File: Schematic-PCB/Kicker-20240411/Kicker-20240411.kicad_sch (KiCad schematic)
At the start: 23 parts, among them J1 Conn_01x02_Pin, J2 Conn_01x05_Pin, J3 Conn_01x02_Pin, Q1 NMOS, U2 TSSP58P38, U3 TSSP58P38, U4 74LVC1G04, U5 74LVC1G04, U6 74AHC1G08

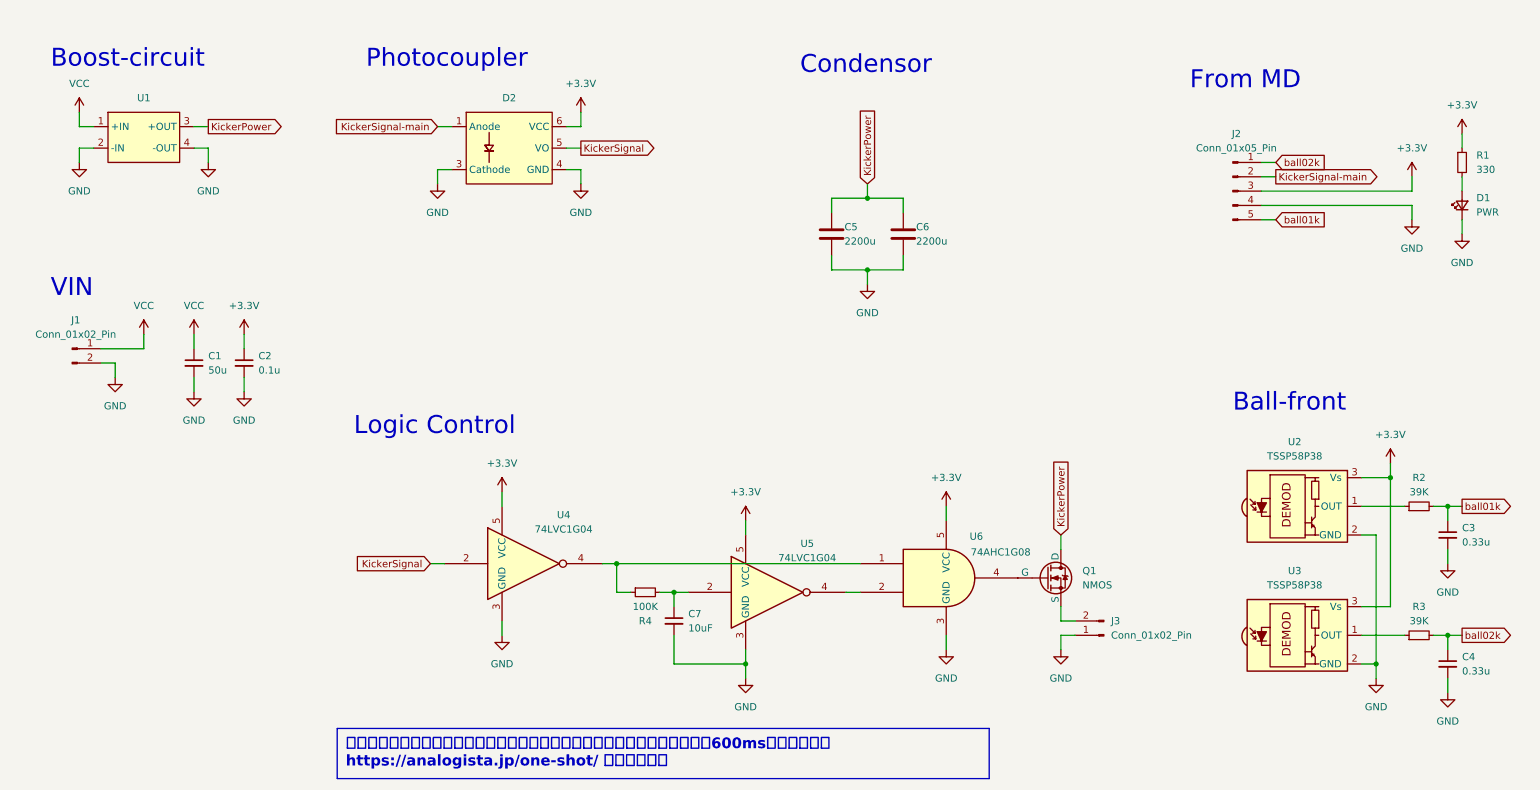
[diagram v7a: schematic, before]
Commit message: キッカー基板 回路図の更新
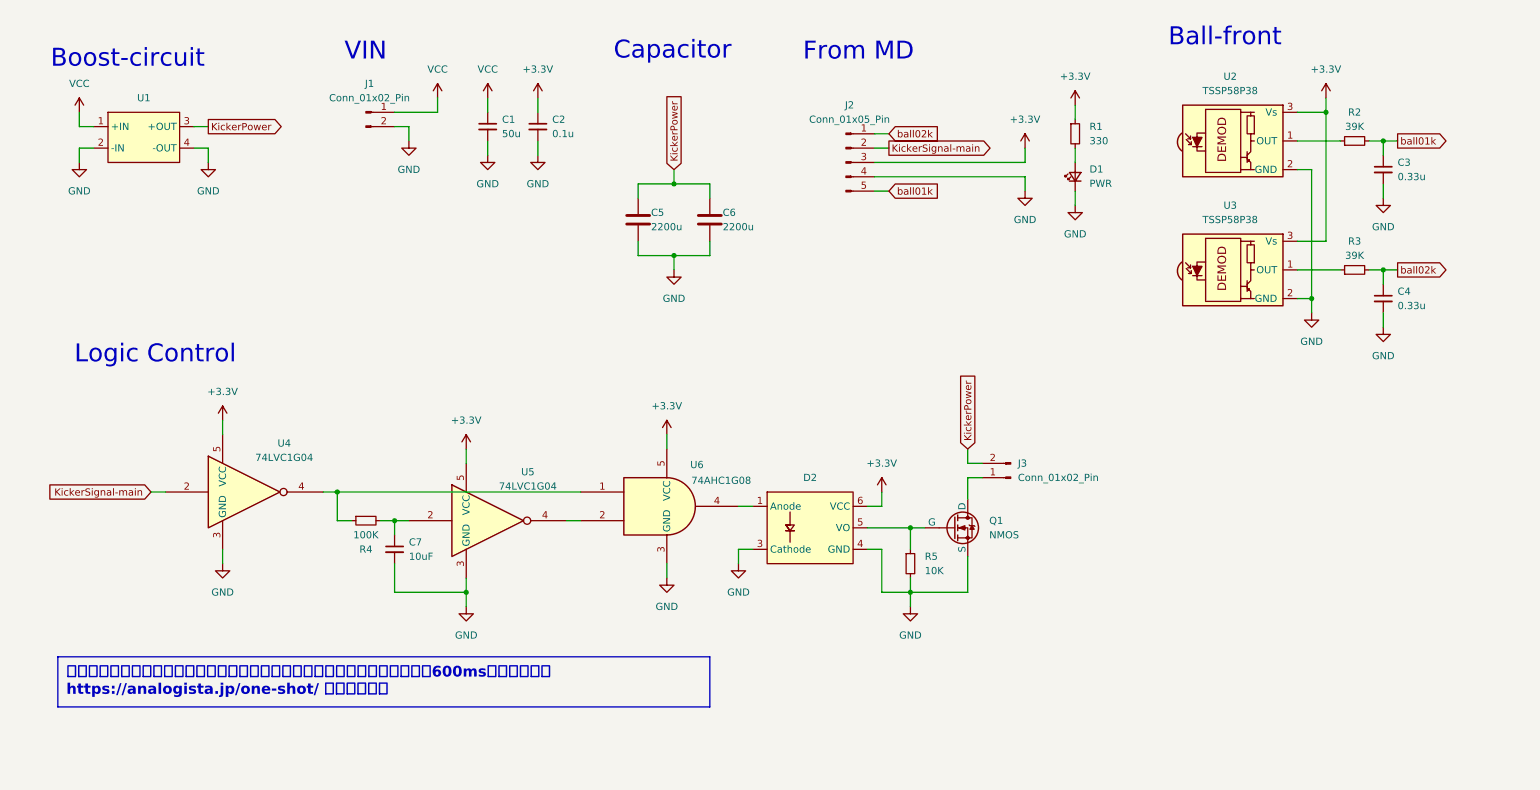
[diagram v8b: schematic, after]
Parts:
- added R5: 10K, symbol Device:R_Small
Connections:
- net GND: now also Q1.3 (S), R5.2; no longer J3.1 (Pin_1)
- net KickerPower: now also J3.2 (Pin_2); no longer Q1.2 (D)
- net KickerSignal-main: now also U4.2; no longer D2.1 (Anode)
- net at U6.4: now also D2.1 (Anode); no longer Q1.1 (G)
- net KickerSignal: no longer names the net of D2.5 (VO)
- net KickerSignal: now also Q1.1 (G), R5.1; no longer U4.2
- new net: J3.1 (Pin_1), Q1.2 (D)
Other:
- note added: "Capacitor"
- note removed: "Condensor"
- note removed: "Photocoupler"
- moved on the sheet: C1, C2, C3, C4, C5, C6, C7, D1, D2, J1, J2, J3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
